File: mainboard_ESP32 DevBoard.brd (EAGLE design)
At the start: 54.9 x 106.7 mm, 44 parts, among them IC1 OP-AMP-2-LONG, IC3 74HC08N, K1 AQH213, X1 JST-XH-02-PIN-LONG-PAD, X2 JST-XH-04-PIN-LONG-PAD, X5 JST-XH-04-PIN-LONG-PAD, X7 1751293

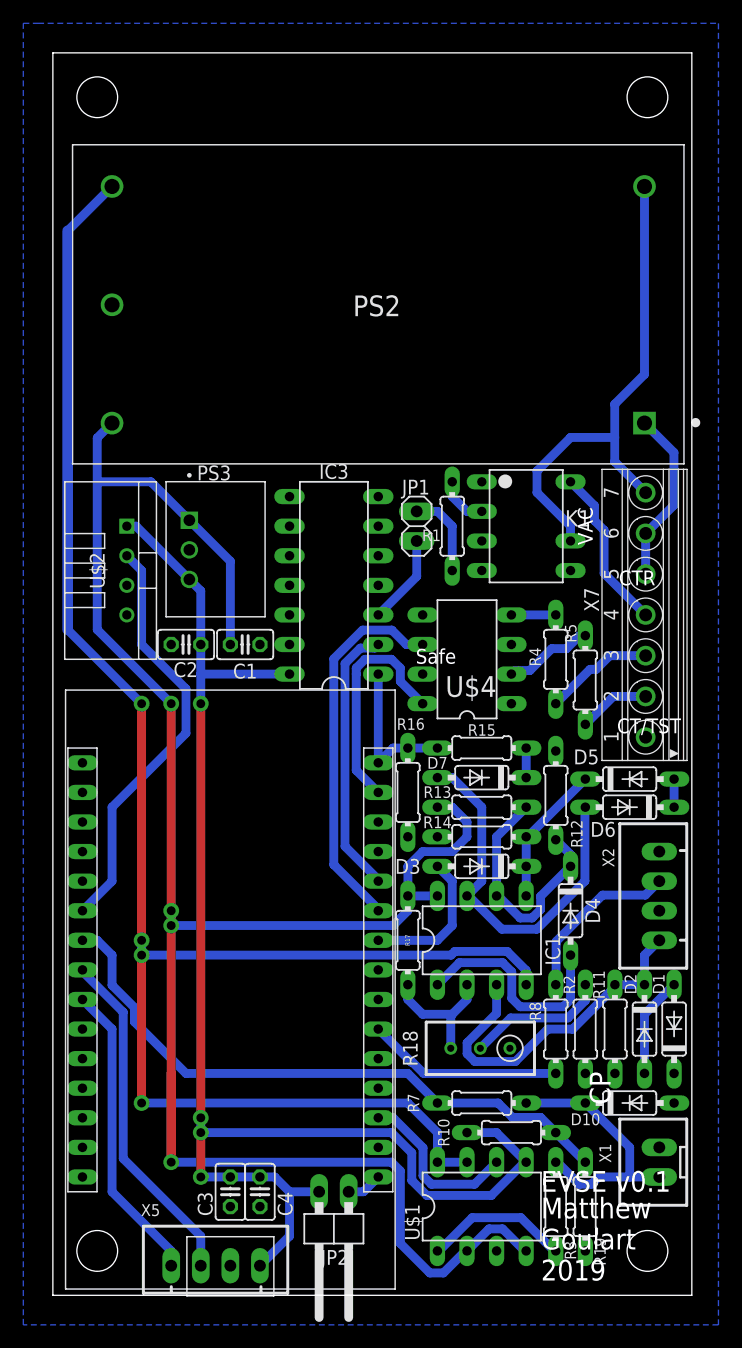
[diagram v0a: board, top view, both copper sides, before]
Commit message: Cleaned labels
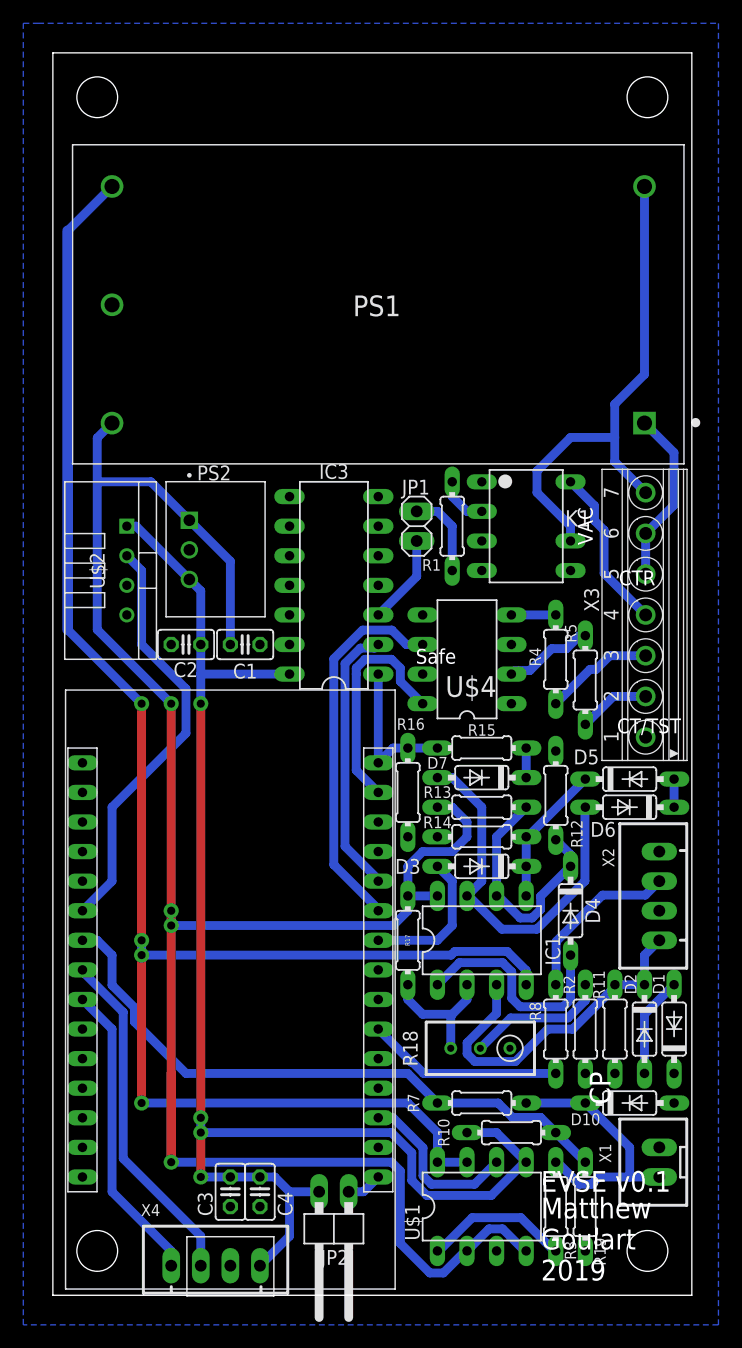
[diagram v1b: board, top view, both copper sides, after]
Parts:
- removed PS3: R-78E3.3-0.5, R-78E3.3-0.5:CONV_R-78E3.3-0.5
- added PS1: RAC20-12DK, RAC20-12DK:CONV_RAC20-12DK
- PS2: value RAC20-12DK -> R-78E3.3-0.5; device RAC20-12DK:CONV_RAC20-12DK -> R-78E3.3-0.5:CONV_R-78E3.3-0.5
- moved PS2 25.3 mm to (14.0, 64.0), turned to 270 degrees
- renumbered X5 to X4, X7 to X3
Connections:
- net +12V: now also PS1.5, PS2.1; no longer PS2.5, PS3.1
- net +3V3: now also PS2.3; no longer PS3.3
- net -12V: now also PS1.3; no longer PS2.3
- net GND: now also PS1.4, PS2.2; no longer PS2.4, PS3.2
- net VACL: now also PS1.2; no longer PS2.2
- net VACN: now also PS1.1; no longer PS2.1

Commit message: Reworked GFCI to account for noise on the line. Swapped out AND gate for 2 mosfets. Removed mostly useless caps from PSU outputs, caps should be closer to devices
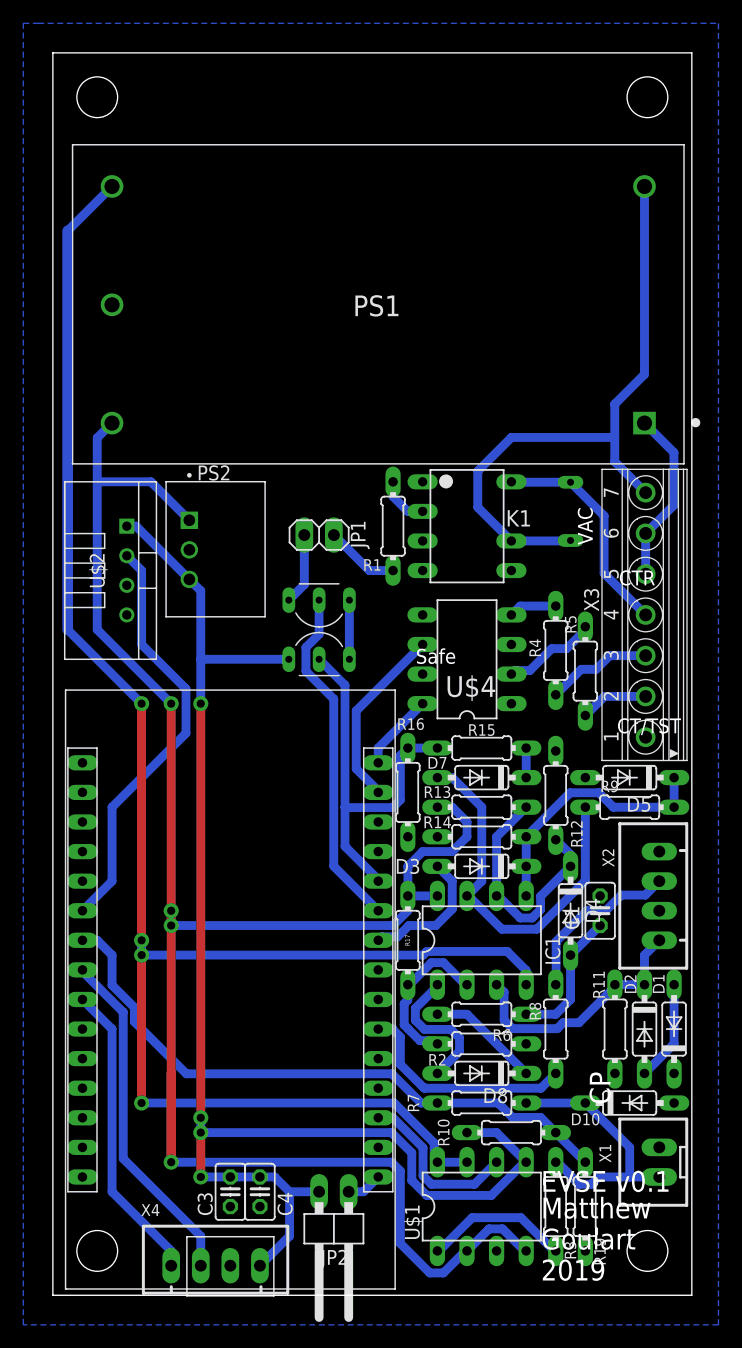
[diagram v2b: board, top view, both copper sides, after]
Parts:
- removed C2: 10uF, rcl:C025-025X050
- removed D6: 1N4148DO35-7, diode:DO35-7
- removed IC3: 74HC08N, 74xx-eu:DIL14
- removed R18: 100, rcl:RTRIM3296W
- added D8: 1N4148DO35-7, diode:DO35-7
- added R6: 1K, Passive:0204/7-L
- added R9: 10K, Passive:0204/7-L
- added U$5: MOV-07D391K, EVSE:DISC-7
- added U$6, U$7: 2N7000, EVSE:TO-92
- C1: value 10uF -> 6uF
- R2: value 560 -> 620
- moved C1 38.1 mm to (47.0, 33.0), turned to 90 degrees
- moved R2 8.98 mm to (36.8, 21.6), turned to 180 degrees
- moved JP1 8.42 mm to (22.9, 65.3), turned to 180 degrees
- moved K1 5.08 mm to (35.6, 66.0)
- moved R1 5.08 mm to (29.2, 66.0)
- moved R4 0.76 mm to (43.2, 55.4)
- moved R5 0.76 mm to (45.7, 53.6)
- moved D5 0.13 mm to (49.5, 44.5), turned to 180 degrees
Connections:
- removed net N$12: D5.A, D6.C
- new net N$15: D8.A, IC1.1
- new net N$18: U$6.P$3, U$7.P$1
- net +12V: no longer C1.1
- net +3V3: now also U$6.P$1; no longer C2.1, IC3.14
- net ENER: now also U$7.P$3; no longer IC3.3
- net ENER_COIL: now also U$5.P$1
- net GFI_INT: now also U$3.GPIO21, U$6.P$2; no longer IC3.1, U$3.GPIO23
- net GND: now also D5.A; no longer C2.2, IC3.7
- net MCU_ENER: now also U$3.GPIO19, U$7.P$2; no longer IC3.2, U$3.GPIO21
- net N$13: now also R9.2
- net N$2: now also R2.2; no longer R18.3
- net N$4: now also R9.1; no longer D6.A
- net N$6: now also D8.C, R6.2; no longer R18.2, R2.2
- net N$9: now also C1.1, R6.1; no longer IC1.1
- net VACL: now also U$5.P$2
- net VACL_SENS: now also U$3.GPIO22; no longer U$3.GPIO19
- net VACN_SENS: now also U$3.GPIO23; no longer U$3.GPIO22
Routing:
- net GFI_INT: track 13.2 -> 33.5 mm
- net VACL_SENS: track 32.4 -> 15.8 mm
- net VACN_SENS: track 19.7 -> 6.66 mm
- net +12V: track 167.4 -> 155.2 mm
- net N$15: track 0.00 -> 12.1 mm
- net VACL: track 43.5 -> 53.7 mm
- net N$13: track 12.3 -> 22.4 mm
- net CT: track 29.7 -> 21.8 mm
- net N$9: track 19.2 -> 11.7 mm
- net MCU_ENER: track 23.4 -> 29.7 mm
- net N$18: track 0.00 -> 5.08 mm
- net ENER_COIL: track 14.1 -> 19.2 mm
- net GFI_TST_SIG: track 16.8 -> 19.3 mm
- net N$12: track 2.41 -> 0.00 mm
- net N$6: track 12.1 -> 9.72 mm
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
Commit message: Re-worked GFCI to be tolerant of transient spikes. Removed some components because of it
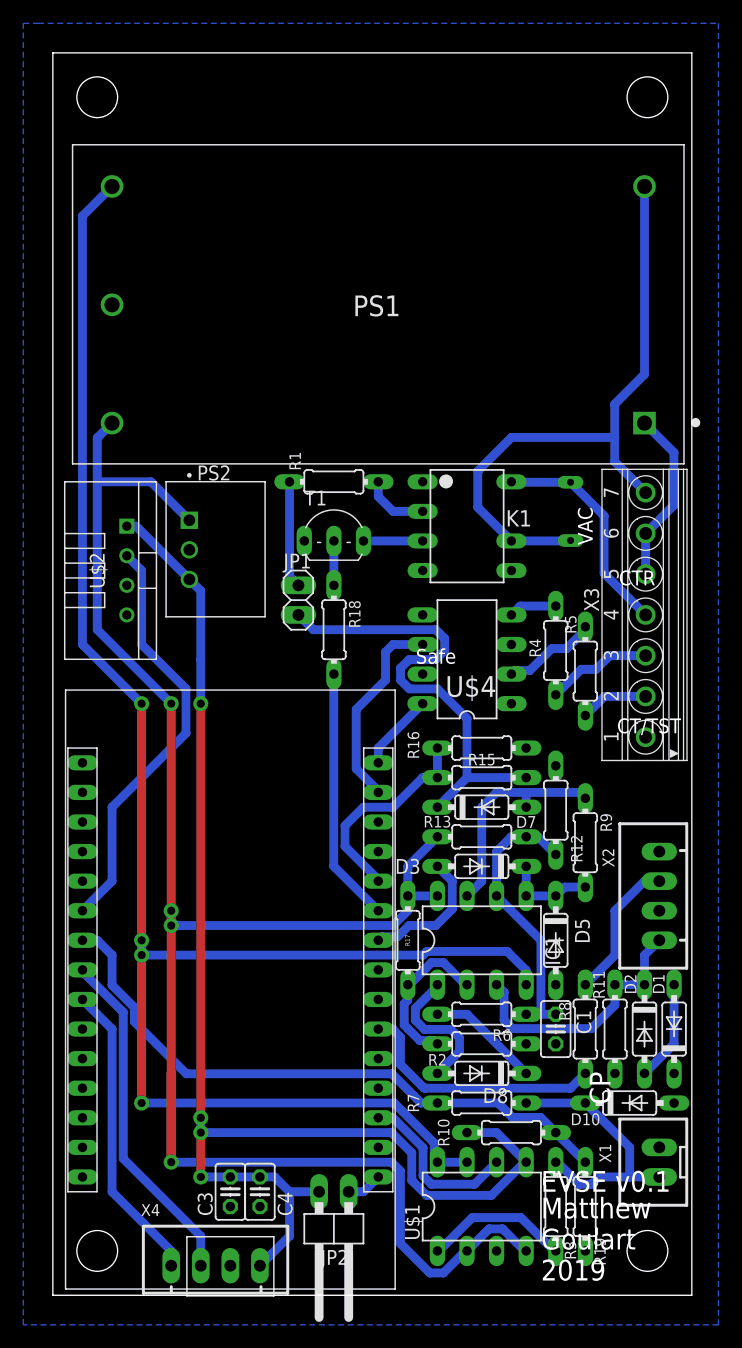
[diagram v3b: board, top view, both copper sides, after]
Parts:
- removed D4: 1N4148DO35-7, diode:DO35-7
- removed R14: 10K, Passive:0204/7-L
- removed U$6, U$7: 2N7000, EVSE:TO-92
- added R18: 3.3K, Passive:0204/7-L
- added T1: 2N2222, transistor-neu-to92:TO92-EBC
- C1: value 6uF -> 5.6uF
- D5: value 1N4148DO35-7 -> 8V; device diode:DO35-7 -> Passive:DO35-7
- R1: value 160 -> 910
- R12: value 2K -> 40K
- R13: value 10K -> 200K
- R6: value 1K -> 1.3K
- R9: value 10K -> 1K
- moved D5 15.3 mm to (43.2, 30.5), turned to 270 degrees
- moved C1 10.9 mm to (43.2, 22.9), turned to 270 degrees
- moved R16 7.41 mm to (36.8, 47.0), turned to 180 degrees
- moved R1 6.35 mm to (24.1, 69.8), turned to 180 degrees
- moved JP1 5.86 mm to (21.1, 59.7), turned to 270 degrees
- moved R9 4.88 mm to (45.7, 38.9), turned to 270 degrees
- moved D7 2.54 mm to (36.8, 41.9), turned to 0 degrees
- moved R13 2.54 mm to (36.8, 39.4)
- moved R15 2.54 mm to (36.8, 44.5)
- moved R8 2.54 mm to (45.7, 22.9)
- moved R12 1.27 mm to (43.2, 41.7)
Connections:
- removed net N$18: U$6.P$3, U$7.P$1
- removed net N$7: D7.C, R15.2
- new net N$12: R18.1, T1.B
- net +3V3: no longer U$6.P$1
- net ENER: now also D7.C, R15.2; no longer U$7.P$3
- net GFI_INT: no longer U$6.P$2
- net GND: now also T1.E; no longer K1.3, R14.1
- net MCU_ENER: now also R18.2; no longer U$7.P$2
- net N$13: no longer R14.2
- net N$14: now also K1.3, T1.C; no longer D4.C, IC1.6, R12.2, R13.1
- net N$9: now also IC1.6, R12.2, R13.1; no longer D4.A
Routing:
- net ENER: track 6.14 -> 40.7 mm
- net N$14: track 21.1 -> 5.08 mm
- net GFI_INT: track 33.5 -> 18.2 mm
- net N$13: track 22.4 -> 7.94 mm
- net N$4: track 32.4 -> 19.2 mm
- net N$9: track 11.7 -> 24.3 mm
- net MCU_ENER: track 29.7 -> 21.9 mm
- net +3V3: track 123.5 -> 115.9 mm
- net +12V: track 155.2 -> 148.4 mm
- net N$18: track 5.08 -> 0.00 mm
- net N$12: track 0.00 -> 3.81 mm
- net N$3: track 6.34 -> 9.21 mm
- net N$7: track 2.54 -> 0.00 mm
- net GFI_TST_SIG: track 19.3 -> 21.8 mm
- net GFI_TEST: track 14.7 -> 12.3 mm
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
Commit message: Completed new GFCI circuit
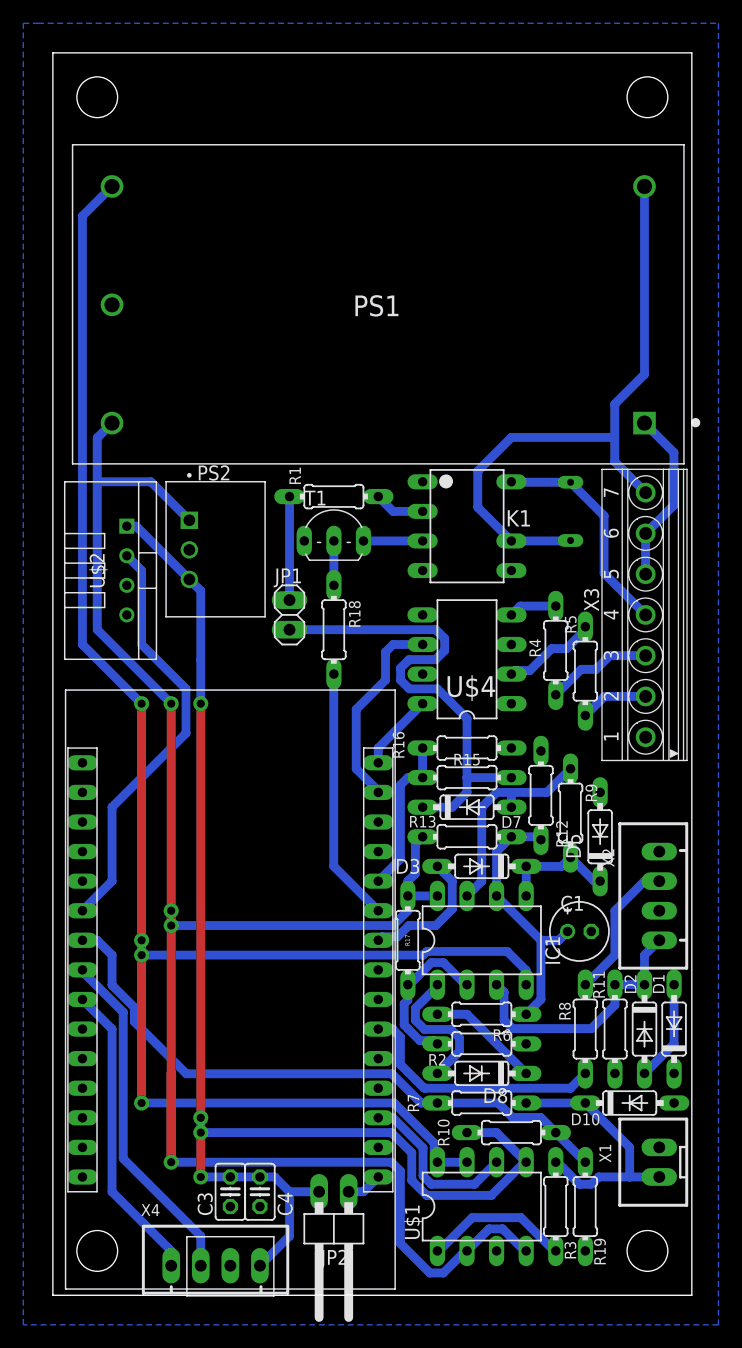
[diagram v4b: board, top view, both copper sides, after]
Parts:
- C1: device rcl:C025-025X050 -> rcl:E2-5
- D1, D2: value 12V -> 10V
- moved D5 9.67 mm to (47.0, 39.4), turned to 90 degrees
- moved C1 8.62 mm to (45.2, 31.2), turned to 0 degrees
- moved R9 2.84 mm to (44.5, 41.4)
- moved R12 1.80 mm to (41.9, 42.9)
- moved JP1 1.48 mm to (20.3, 58.4)
- moved D7 1.27 mm to (35.6, 41.9)
- moved R1 1.27 mm to (24.1, 68.6)
- moved R13 1.27 mm to (35.6, 39.4)
- moved R15 1.27 mm to (35.6, 44.5)
- moved R16 1.27 mm to (35.6, 47.0)
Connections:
- net GND: now also C1.-; no longer C1.2
- net N$9: now also C1.+; no longer C1.1
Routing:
- net GFI_INT: track 18.2 -> 13.8 mm
- net N$13: track 7.94 -> 10.0 mm
- net N$1: track 5.61 -> 4.34 mm
- net N$9: track 24.3 -> 23.1 mm
- net ENER: track 40.7 -> 41.7 mm
- net N$4: track 19.2 -> 18.4 mm
- net +12V: track 148.4 -> 147.8 mm
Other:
- board text removed: "CP"
- board text removed: "CT/TST"
- board text removed: "CTR"
- board text removed: "EVSE v0.1"
- board text removed: "Matthew Goulart 2019"
- board text removed: "Safe"
- board text removed: "VAC"
